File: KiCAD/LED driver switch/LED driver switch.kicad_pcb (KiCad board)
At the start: 2 copper layers, 10 parts, among them Q1 TN2124, Q2 PMOS, U1 Itsy_Bitsy_32u4

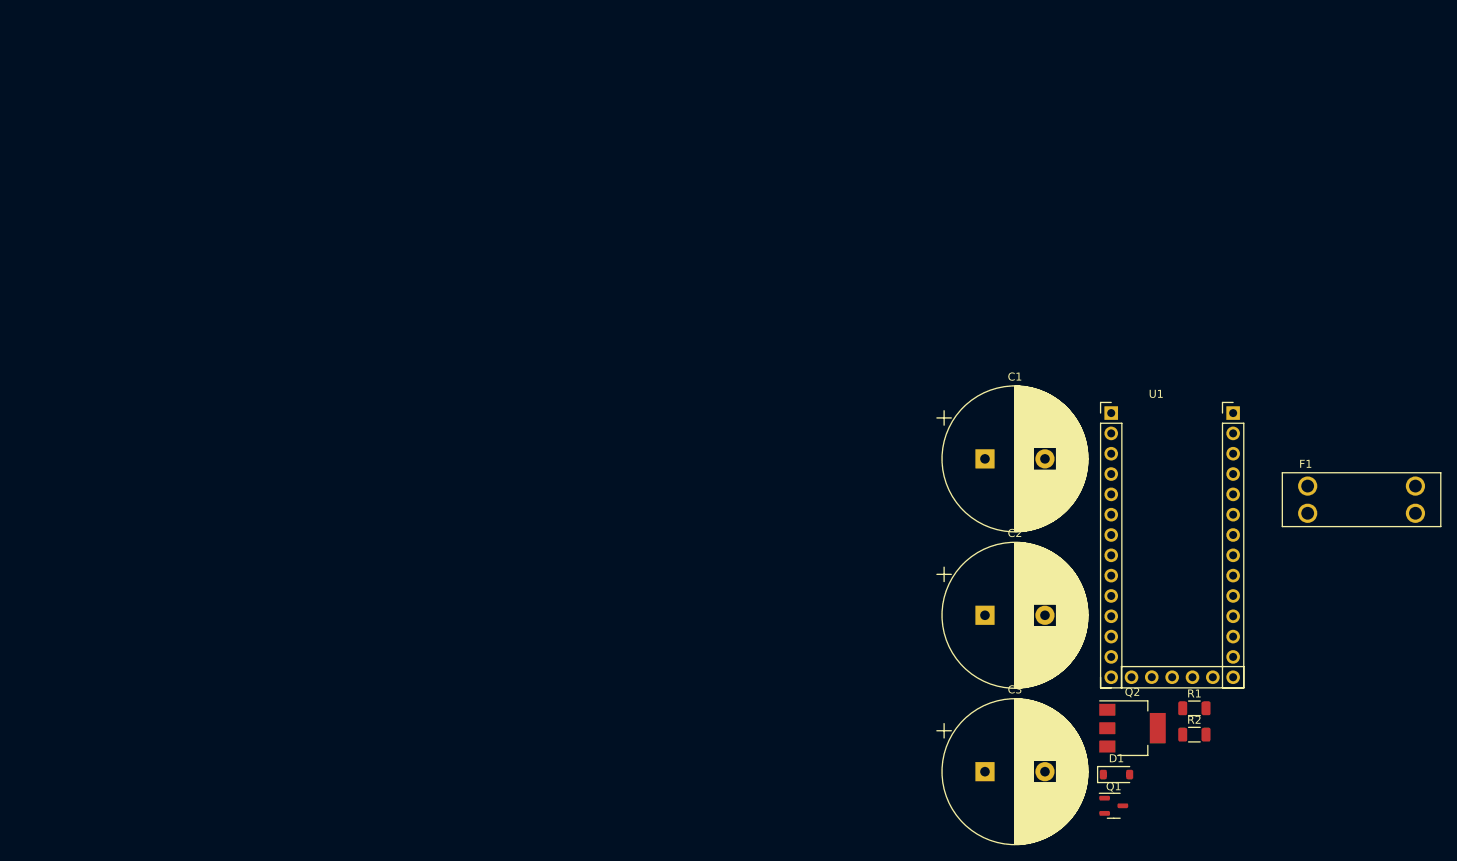
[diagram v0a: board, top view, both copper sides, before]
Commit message: Working PCB draft
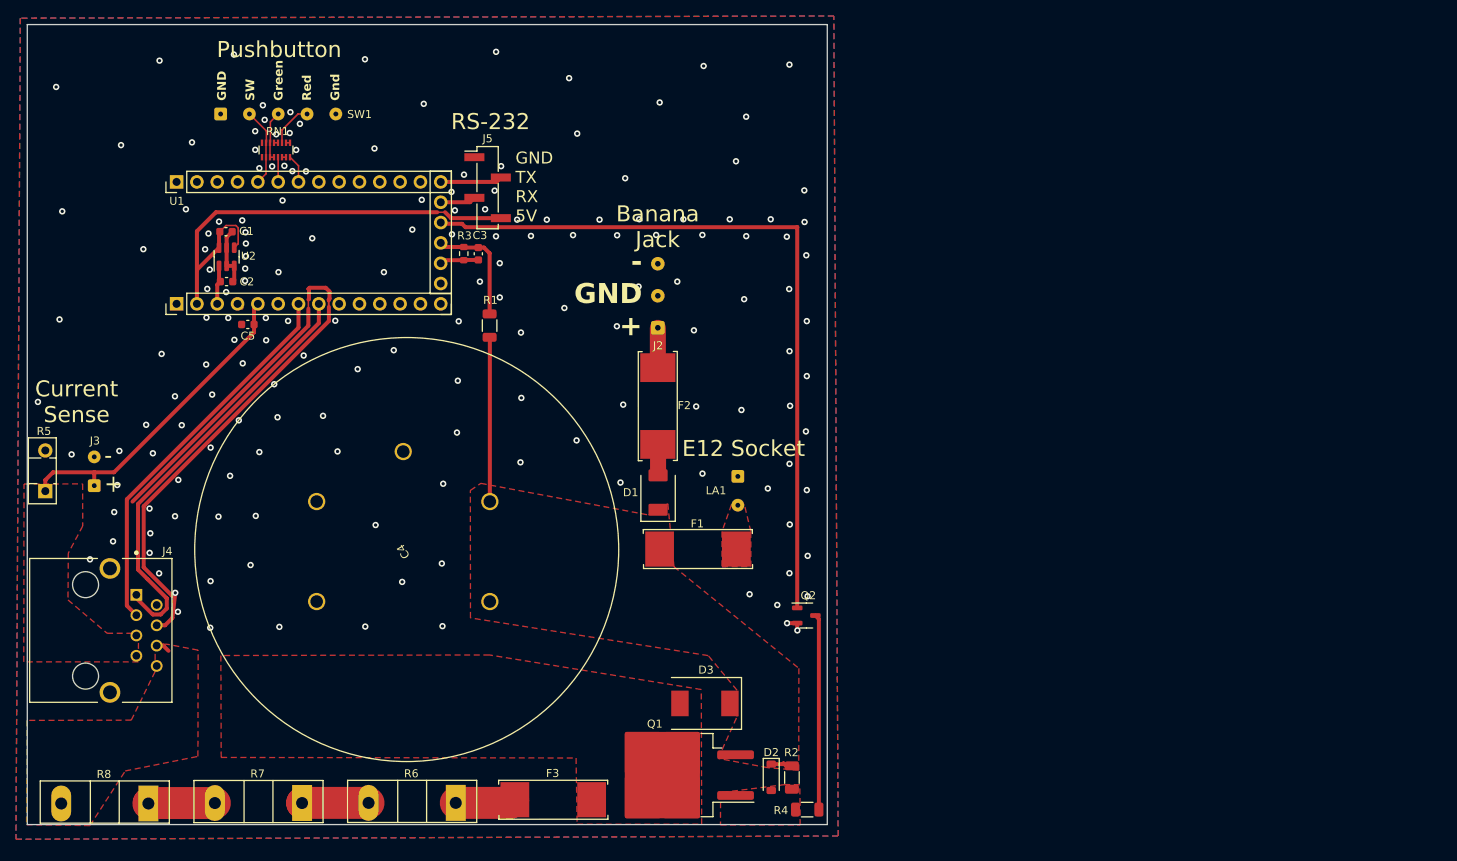
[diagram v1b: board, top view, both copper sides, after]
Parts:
- added C4: 3mF, Custom footprints:ALF20G302KP400, F.Cu at (56.2, 87.1)
- added C5: 1nF, Capacitor_SMD:C_0603_1608Metric, F.Cu at (47.6, 52.5)
- added D2: 15V Zener, Diode_SMD:D_SOD-123, F.Cu at (113.0, 109.1)
- added D3: TVS, Custom footprints:SMDJSeries_LTF, F.Cu at (104.7, 99.9)
- added F2: Fuse, Custom footprints:FUSE_OMF250_SCH, F.Cu at (98.8, 62.1)
- added F3: Fuse, Custom footprints:FUSE_OMF250_SCH, F.Cu at (85.2, 111.9)
- added J2: 3x Banana Jack, Connector_Wire:SolderWire-0.15sqmm_1x03_P4mm_D0.5mm_OD1.5mm, F.Cu at (98.8, 52.9)
- added J3: Conn_Coaxial, Connector_Wire:SolderWire-0.1sqmm_1x02_P3.6mm_D0.4mm_OD1mm, F.Cu at (28.4, 72.6)
- added J4: 8P8C_Shielded, Custom footprints:BEL_SS71800-019F, F.Cu at (27.3, 90.7)
- added J5: Conn_01x04_Pin, Connector_PinHeader_2.54mm:PinHeader_1x04_P2.54mm_Vertical_SMD_Pin1Left, F.Cu at (77.5, 35.4)
- added LA1: E12 Socket, Connector_Wire:SolderWire-0.1sqmm_1x02_P3.6mm_D0.4mm_OD1mm, F.Cu at (108.8, 71.5)
- added R3: 20k, Resistor_SMD:R_0603_1608Metric, F.Cu at (74.6, 43.6)
- added R4: 100k, Resistor_SMD:R_1206_3216Metric, F.Cu at (117.5, 113.1)
- added R5: 1, Package_TO_SOT_THT:TO-126-2_Vertical, F.Cu at (22.3, 73.3)
- added R6: 10, Package_TO_SOT_THT:TO-247-2_Vertical, F.Cu at (73.6, 112.3)
- added R7: 10, Package_TO_SOT_THT:TO-247-2_Vertical, F.Cu at (54.4, 112.3)
- added R8: 10, Package_TO_SOT_THT:TO-247-2_Vertical, F.Cu at (35.1, 112.4)
- added RN1: R_Pack08, Resistor_SMD:R_Array_Convex_8x0602, F.Cu at (51.1, 30.7)
- added SW1: SW_Push_LED, Connector_Wire:SolderWire-0.1sqmm_1x05_P3.6mm_D0.4mm_OD1mm, F.Cu at (44.2, 26.2)
- added SYM1: SYM_Flash_Small, Custom footprints:Symbol_HighVoltage, B.Cu at (67.1, 79.2)
- added U2: 4.096V, Package_TO_SOT_SMD:SOT-23-6, F.Cu at (44.9, 44.0)
- C1: value 100µF -> 2.2µF; footprint Capacitor_THT:CP_Radial_D18.0mm_P7.50mm -> Capacitor_SMD:C_0603_1608Metric
- C2, C3: value 100µF -> 1nF; footprint Capacitor_THT:CP_Radial_D18.0mm_P7.50mm -> Capacitor_SMD:C_0603_1608Metric
- D1: value 15V Zener -> D; footprint Diode_SMD:D_SOD-123 -> Custom footprints:P26_DO-214AA_SMB
- F1: footprint Custom footprints:FUSE_3557-15 -> Custom footprints:FUSE_OMF250_SCH
- Q1: value TN2124 -> PMOS; footprint Package_TO_SOT_SMD:SOT-23-3 -> Package_TO_SOT_SMD:TO-263-2
- Q2: value PMOS -> TN2124; footprint Package_TO_SOT_SMD:SOT-223-3_TabPin2 -> Package_TO_SOT_SMD:SOT-23-3
- R1: value 100k -> 1M
- moved U1 122.5 mm to (35.4, 48.1), turned to 90 degrees
- moved C2 103.6 mm to (44.9, 47.1)
- moved R1 100.2 mm to (77.8, 52.6), turned to 90 degrees
- moved C1 99.0 mm to (44.8, 40.9)
- moved C3 90.6 mm to (76.4, 43.6), turned to -90 degrees
- moved F1 82.6 mm to (104.4, 80.6), turned to 180 degrees
- moved D1 66.2 mm to (98.8, 75.7), turned to 90 degrees
- moved Q1 55.1 mm to (100.9, 108.8), turned to 180 degrees
- moved R2 50.6 mm to (115.6, 109.1), turned to -90 degrees
- moved Q2 43.1 mm to (117.4, 88.9)
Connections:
- C1 pad 1: /0-200V -> +5V
- C2 pad 1: /0-200V -> /Aref
- C3 pad 1: /0-200V -> /Vsense
- D1 pad 1: Net-(D1-K) -> /0-200V
- D1 pad 2: /0-200V -> Net-(D1-A)
- F1 pad 1: unconnected-(F1-Pad1) -> Net-(LA1-R2.1)
- Q1 pad 1: unconnected-(Q1-G-Pad1) -> Net-(D2-A)
- Q1 pad 2: GND -> Net-(D3-A)
- Q1 pad 3: Net-(Q1-D) -> /0-200V
- Q2 pad 1: Net-(D1-K) -> /LED_trigger
- Q2 pad 2: Net-(D2-A) -> GND
- Q2 pad 3: /0-200V -> Net-(Q2-D)
- R1 pad 1: Net-(D1-K) -> /0-200V
- R1 pad 2: Net-(Q1-D) -> /Vsense
- R2 pad 2: Net-(D1-K) -> Net-(D2-A)
- U1 pad 17: /SW2 -> /Vsense
- U1 pad 18: unconnected-(U1-6_A7-Pad18) -> /LED_trigger
- U1 pad 19: unconnected-(U1-4_A6-Pad19) -> /RS-232 Rx
- U1 pad 20: unconnected-(U1-0_RX-Pad20) -> /RS-232 Tx
- U1 pad 27: unconnected-(U1-~10_A10-Pad27) -> /Red_LED
- U1 pad 28: unconnected-(U1-~11-Pad28) -> /Green_LED
- U1 pad 29: unconnected-(U1-12_A11-Pad29) -> /Pushbutton
- U1 pad 3: GND -> /Aref
- U1 pad 5: unconnected-(U1-18_A0-Pad5) -> /Isense
- U1 pad 7: unconnected-(U1-20_A2-Pad7) -> /Trap door sensor
- U1 pad 8: unconnected-(U1-21_A3-Pad8) -> /Door safety interlock
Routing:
- net GND: track 0.00 -> 109.2 mm, vias 0 -> 169
- net /LED_trigger: track 0.00 -> 92.4 mm
- net +5V: track 0.00 -> 59.7 mm
- net /Door safety interlock: track 0.00 -> 54.3 mm
- net /Trap door sensor: track 0.00 -> 48.3 mm
- net /Isense: track 0.00 -> 40.6 mm
- net Net-(Q2-D): track 0.00 -> 24.7 mm
- net /0-200V: track 0.00 -> 23.3 mm
- net /Vsense: track 0.00 -> 14.2 mm
- net /Pushbutton: track 0.00 -> 9.81 mm
- net Net-(R7-Pad2): track 0.00 -> 8.33 mm
- net Net-(R6-Pad2): track 0.00 -> 8.32 mm
- net /RS-232 Tx: track 0.00 -> 7.74 mm
- net Net-(F3-Pad1): track 0.00 -> 7.35 mm
- net Net-(RN1-R5.2): track 0.00 -> 6.33 mm
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- added copper zone on F.Cu, net /0-200V
- added copper zone on F.Cu, net /Isense
- added copper zone on F.Cu, net /LED+
- added copper zone on B.Cu, net GND
- added copper zone on F.Cu, net GND
- added copper zone on F.Cu, net Net-(D2-A)
- added copper zone on F.Cu, net Net-(D3-A)
- added copper zone on F.Cu, net Net-(LA1-R2.1)
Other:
- board outline added: 100 x 100 mm
- board text added: "- +"
- board text added: "- GND +"
- board text added: "Banana Jack"
- board text added: "Current Sense"
- board text added: "DANGER!"
- board text added: "E12 Socket"
- board text added: "GND SW Green Red Gnd"
- board text added: "GND TX RX 5V"
- board text added: "HIGH VOLTAGE"
- board text added: "Pushbutton"
- board text added: "RS-232"

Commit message: Controller moved - DRC pass
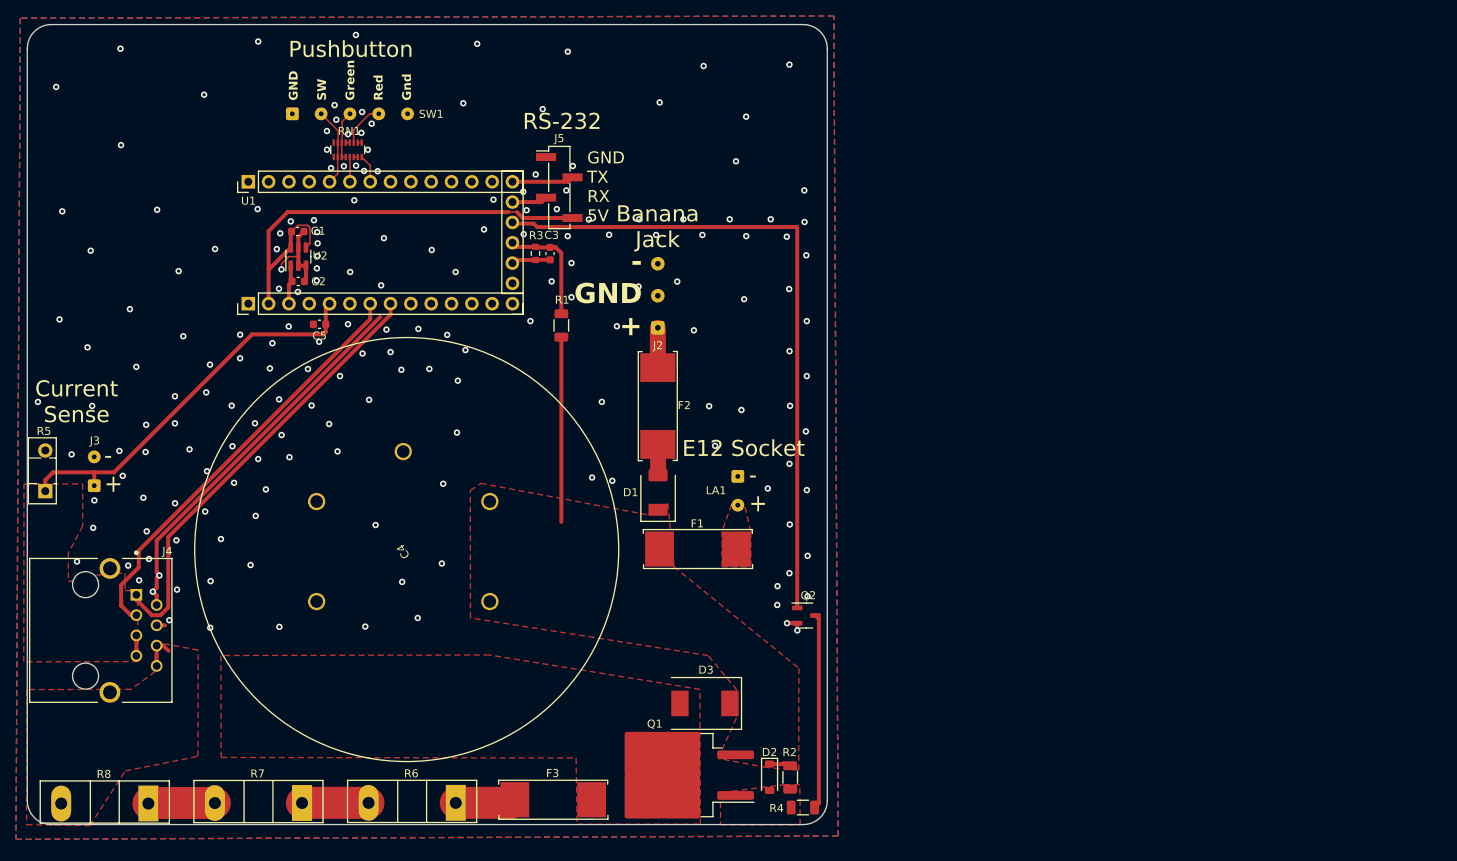
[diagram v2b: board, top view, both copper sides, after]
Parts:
- moved C2 8.97 mm to (53.9, 47.1)
- moved C3 8.97 mm to (85.3, 43.6)
- moved R3 8.97 mm to (83.5, 43.6)
- moved C1 8.97 mm to (53.8, 40.9)
- moved C5 8.97 mm to (56.5, 52.5)
- moved RN1 8.97 mm to (60.1, 30.7)
- moved SW1 8.97 mm to (53.1, 26.2)
- moved U1 8.97 mm to (44.3, 48.1)
- moved U2 8.97 mm to (53.9, 44.0)
- moved J5 8.97 mm to (86.5, 35.4)
- moved R1 8.97 mm to (86.8, 52.6)
- moved R4 0.60 mm to (117.0, 112.9)
- moved D2 0.21 mm to (112.8, 109.1)
- moved R2 0.21 mm to (115.4, 109.1)
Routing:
- net GND: track 109.2 -> 67.1 mm, vias 169 -> 185
- net /Isense: track 40.6 -> 52.1 mm
- net /LED_trigger: track 92.4 -> 83.4 mm
- net /Trap door sensor: track 48.3 -> 53.0 mm
- net /0-200V: track 23.3 -> 25.9 mm
- net /LED+: track 1.74 -> 4.28 mm
- net /Door safety interlock: track 54.3 -> 55.3 mm
- net /Aref: track 5.52 -> 4.97 mm
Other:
- outline, holes or cut-outs redrawn

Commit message: standoffs and enclosure added
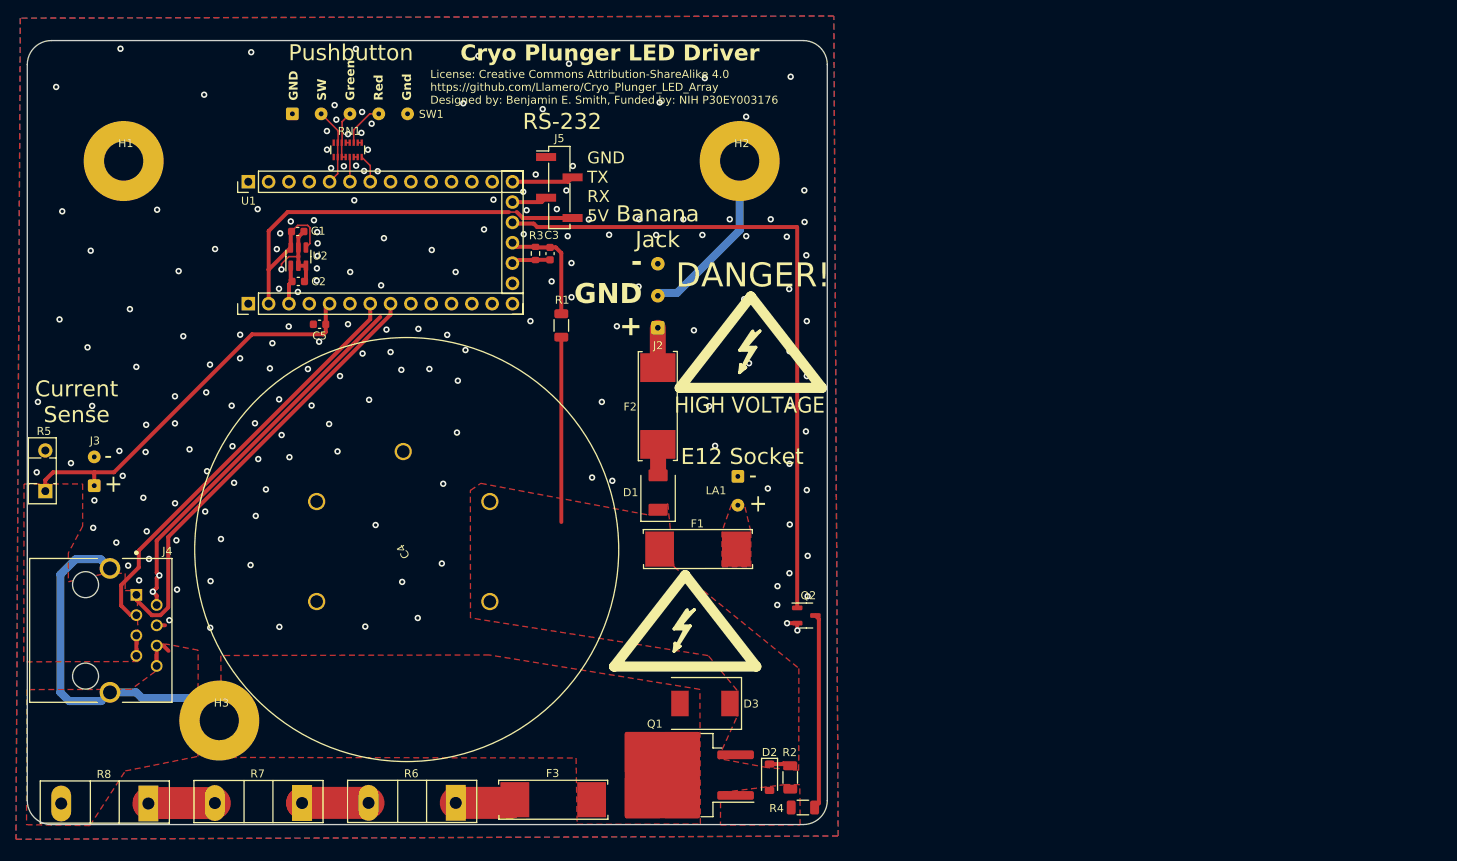
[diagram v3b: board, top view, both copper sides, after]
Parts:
- added H1: Standoff, Custom footprints:8-32 Standoff, F.Cu at (32.0, 32.0)
- added H2: Standoff, Custom footprints:8-32 Standoff, F.Cu at (109.0, 32.0)
- added H3: Standoff, Custom footprints:8-32 Standoff, F.Cu at (44.0, 101.9)
- added SYM2: SYM_Flash_Small, Symbol:Symbol_Highvoltage_Type2_CopperTop_Small, F.Cu at (102.2, 91.4)
- added SYM2: SYM_Flash_Small, Symbol:Symbol_Highvoltage_Type2_CopperTop_Small, F.Cu at (110.4, 56.6)
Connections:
- J2 pad e: /Power supply+ -> (no net)
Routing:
- net Earth_Protective: track 0.00 -> 66.6 mm
- net GND: vias 185 -> 184
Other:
- board size 100 x 100 mm -> 100 x 98 mm
- board text added: "Cryo Plunger LED Driver"
- board text added: "License: Creative Commons Attribution-ShareAlike 4.0 https://github.com/Llamero/Cryo_Plunger_LED_Array Designed by: Benjamin E. Smith, Funded by: NIH P30EY003176"

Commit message: Add pulldown to gate, move LED pin to PWM
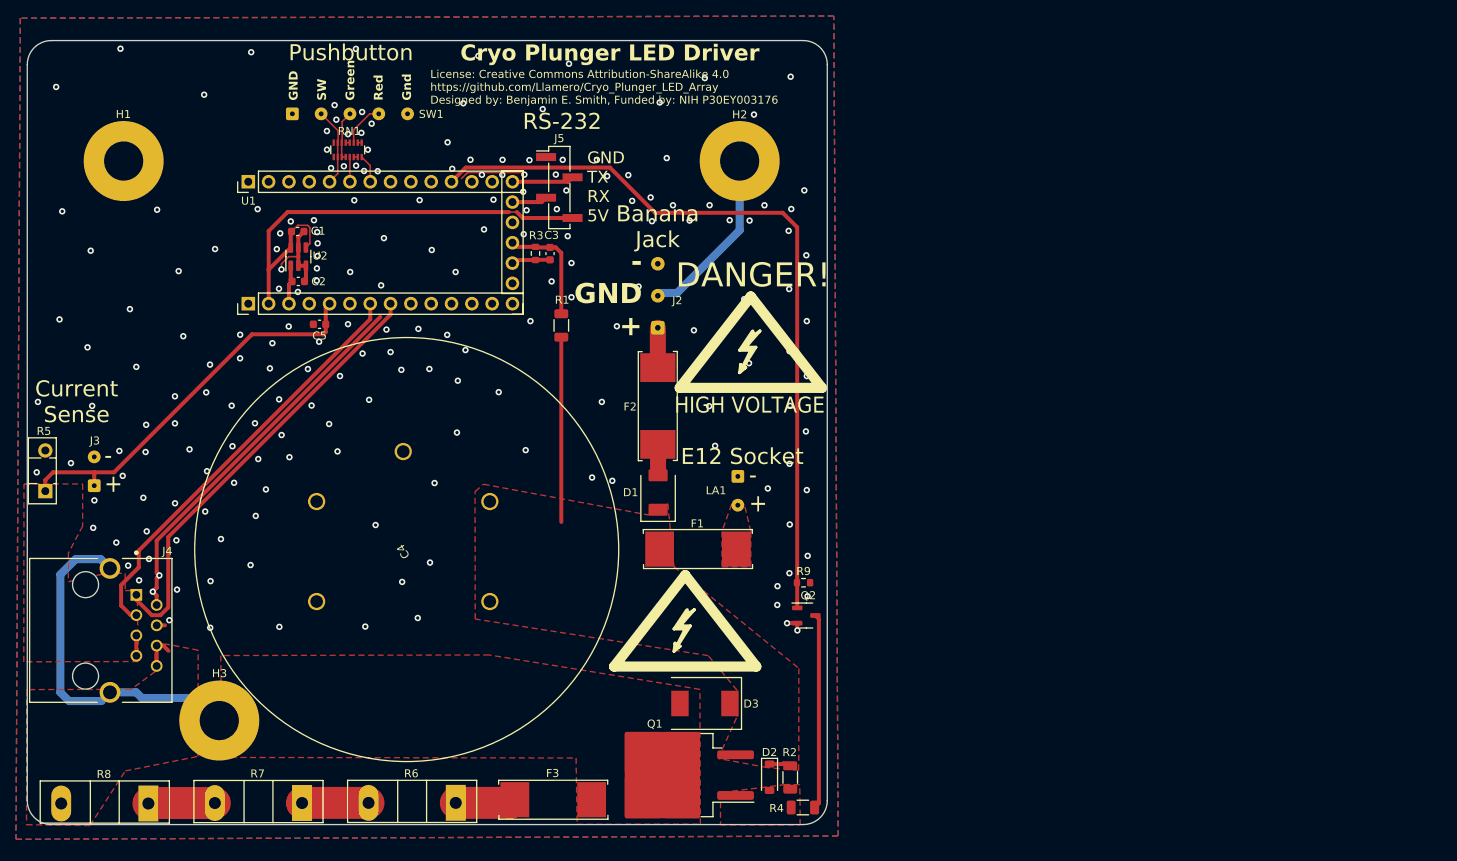
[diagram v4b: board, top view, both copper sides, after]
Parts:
- added R9: 20k, Resistor_SMD:R_0603_1608Metric, F.Cu at (117.0, 84.8)
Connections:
- U1 pad 18: /LED_trigger -> unconnected-(U1-6_A7-Pad18)
- U1 pad 23: unconnected-(U1-~3_SCL-Pad23) -> /LED_trigger
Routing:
- net /LED_trigger: track 83.4 -> 94.6 mm
- net GND: track 67.1 -> 75.4 mm, vias 184 -> 198
